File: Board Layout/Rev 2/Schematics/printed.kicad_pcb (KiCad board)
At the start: 2 copper layers, 5 parts

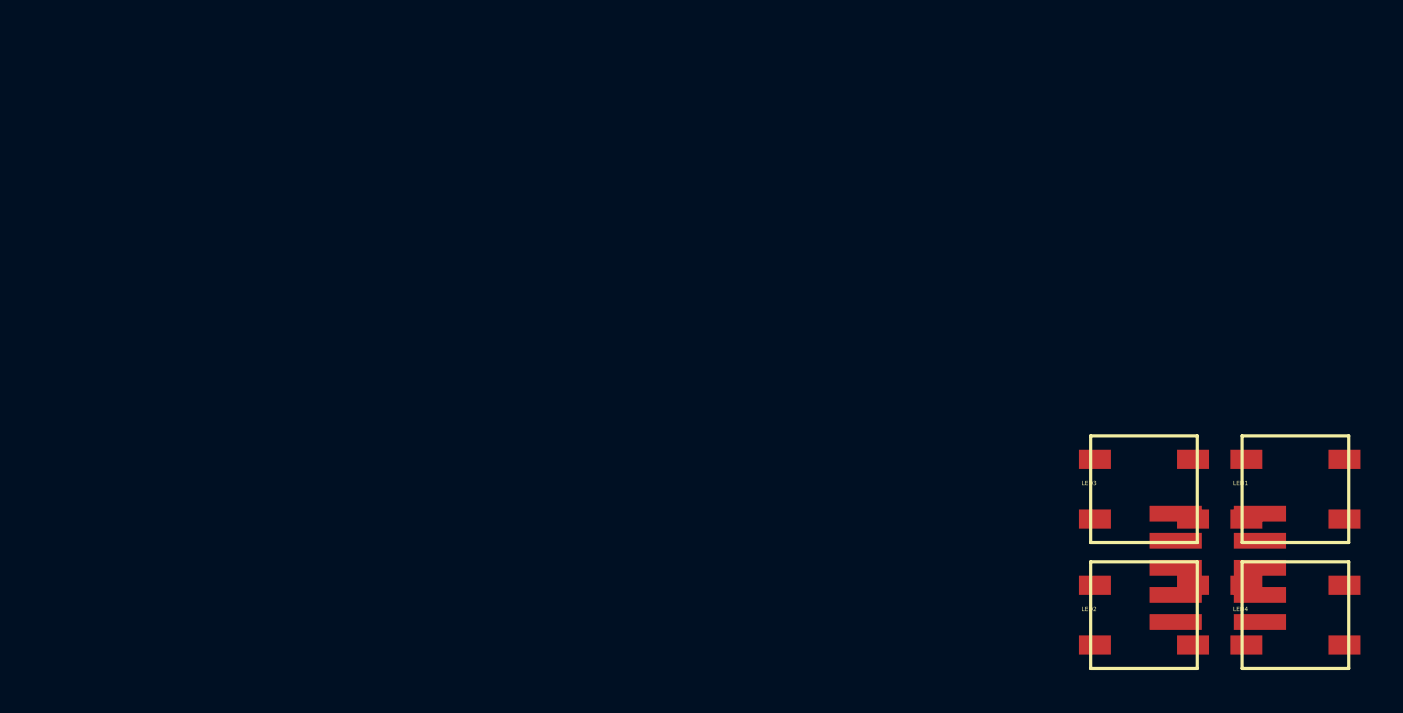
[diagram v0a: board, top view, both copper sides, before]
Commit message: Board Update
not sure if I can do 2 layer as it is too condensed. Might need to
switch to 4 layer.
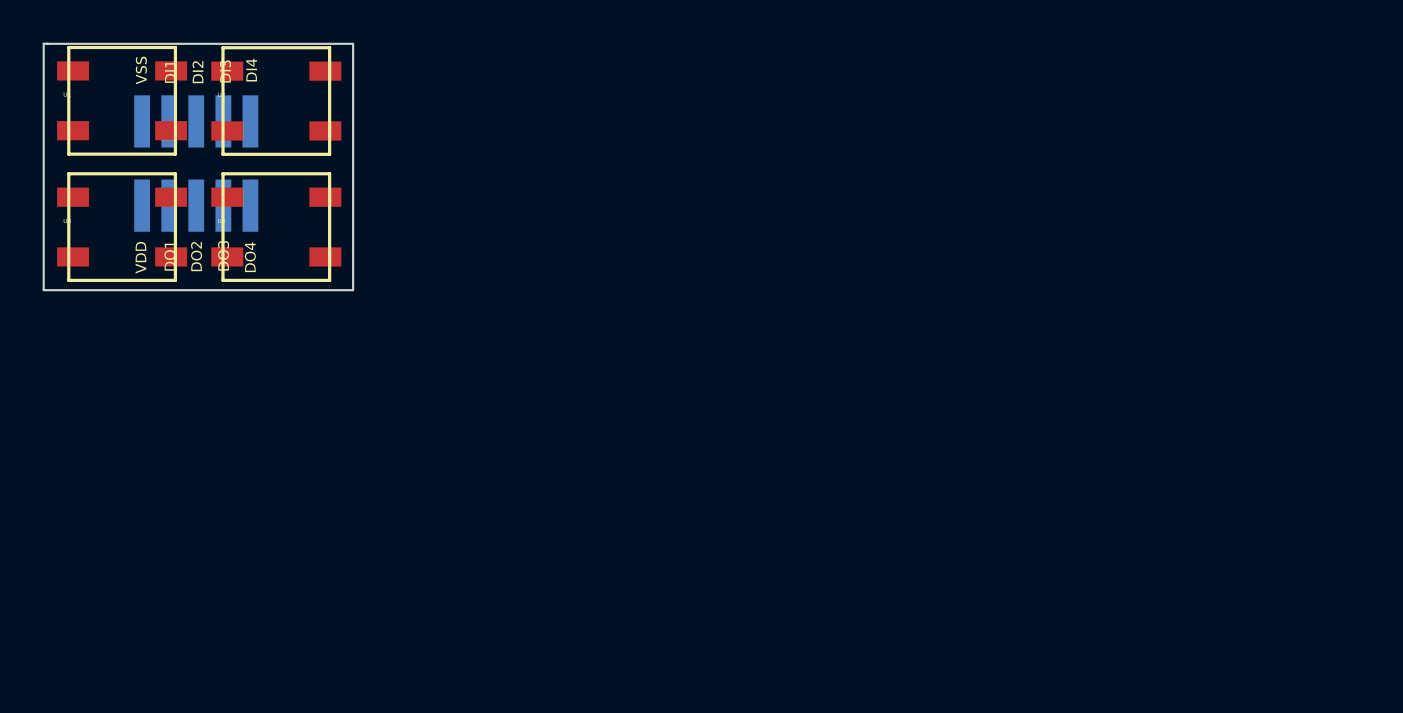
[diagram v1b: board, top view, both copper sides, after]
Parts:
- removed LED1, LED2, LED3, LED4: WS2812B, WS2812B
- added U1: , WS2812B, F.Cu at (118.8, 87.9)
- added U2: , WS2812B, F.Cu at (126.0, 87.9)
- added U3: , WS2812B, F.Cu at (118.8, 93.8)
- added U4: , WS2812B, F.Cu at (126.0, 93.8)
- ?: value CONN_5X2 -> (none); moved to F.Cu
- moved ? 48.7 mm to (128.0, 87.2), turned to 0 degrees
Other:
- board outline added: 14.5 x 11.6 mm

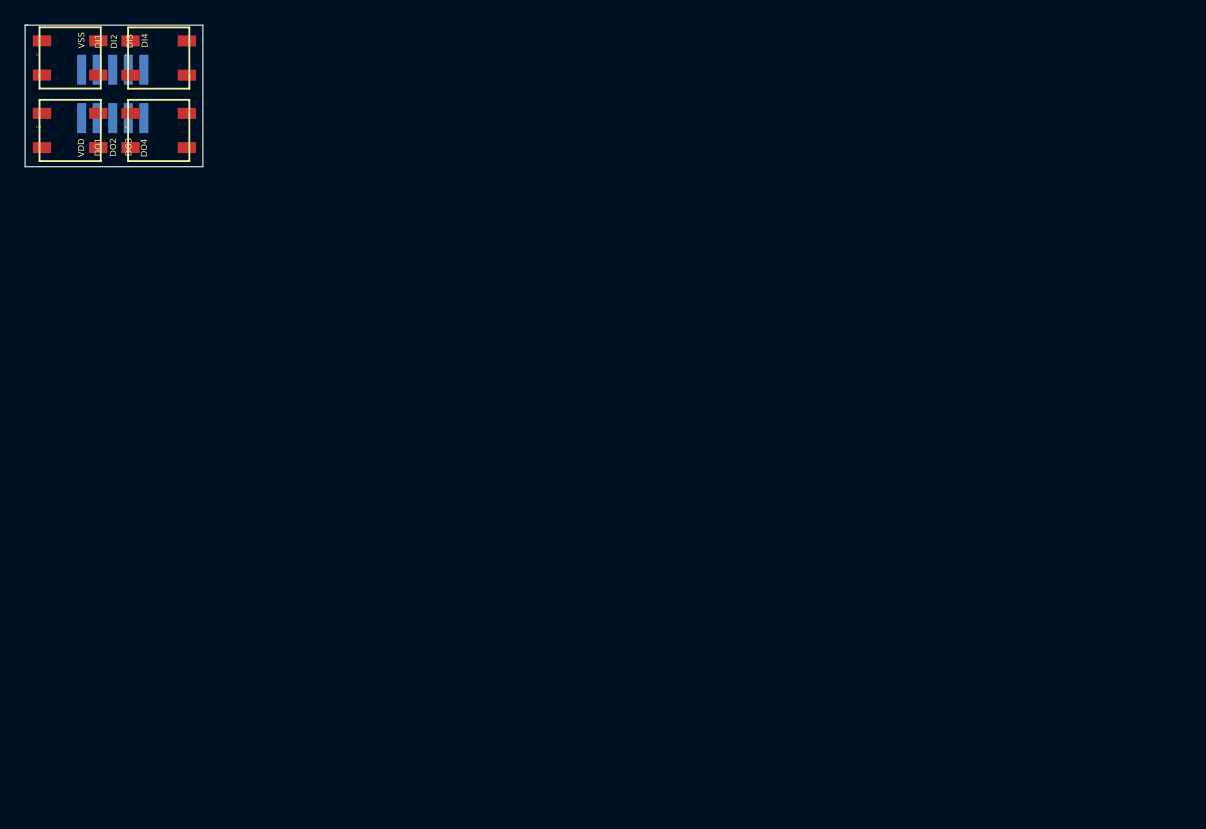
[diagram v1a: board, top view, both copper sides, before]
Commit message: Layout Completion
Verify design is fine via traces and via's; then order. Smaller than v1
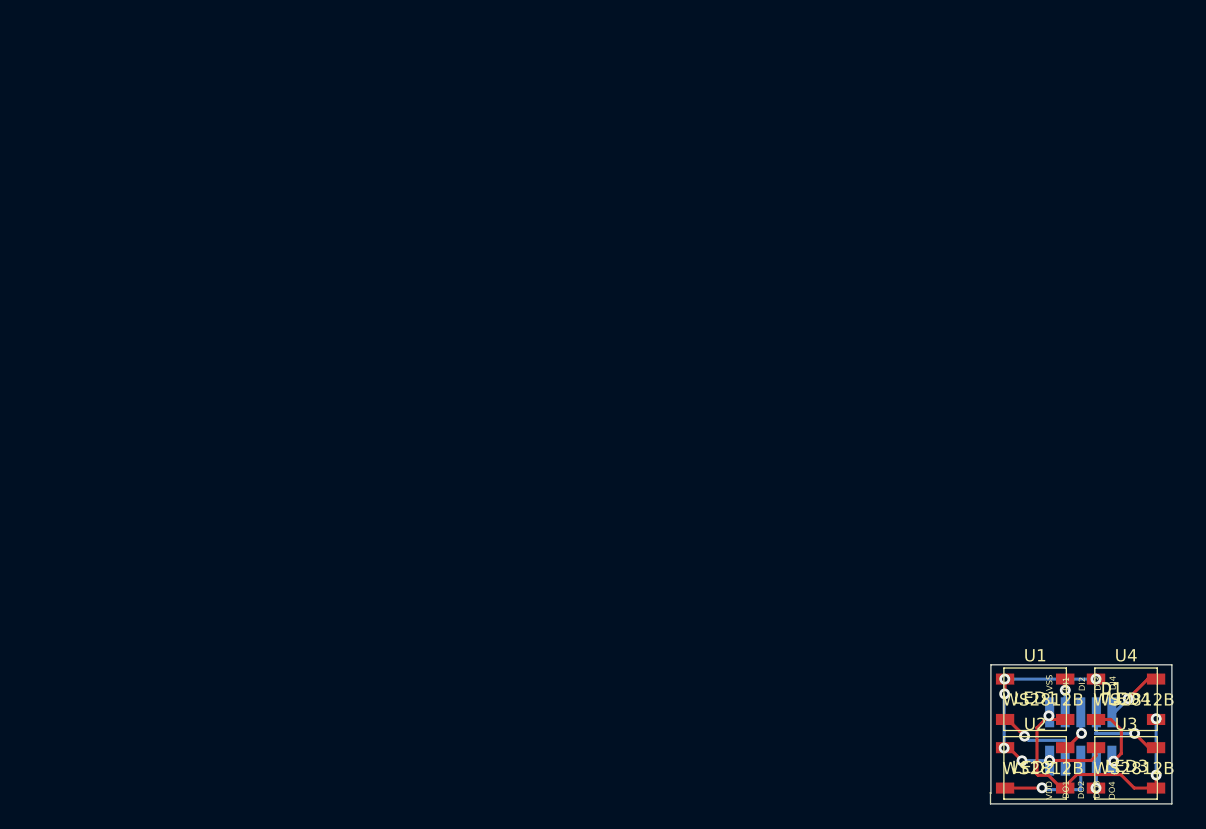
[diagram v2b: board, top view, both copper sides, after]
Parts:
- removed ?: , 10PSMTHdr
- added P1: CONN_5X2, 10PSMTHdr, F.Cu at (207.0, 139.7)
- U1, U2, U3, U4: value (none) -> WS2812B
- moved U3 101.6 mm to (207.5, 143.2)
- moved U1 95.4 mm to (200.1, 137.6)
- moved U4 92.6 mm to (207.5, 137.6)
- moved U2 92.5 mm to (200.1, 143.2)
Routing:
- net N-000006: track 0.00 -> 24.3 mm, vias 0 -> 3
- net N-0000010: track 0.00 -> 21.9 mm, vias 0 -> 6
- net N-000007: track 0.00 -> 8.60 mm, vias 0 -> 1
- net N-000009: track 0.00 -> 7.28 mm, vias 0 -> 1
- net N-000005: track 0.00 -> 7.18 mm, vias 0 -> 1
- net N-000003: track 0.00 -> 5.39 mm, vias 0 -> 1
- net N-000008: track 0.00 -> 4.73 mm, vias 0 -> 1
- net N-000002: track 0.00 -> 3.56 mm, vias 0 -> 1
- net N-000004: track 0.00 -> 2.72 mm, vias 0 -> 1
- net N-000001: track 0.00 -> 2.25 mm, vias 0 -> 1
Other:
- board size 14.5 x 11.6 mm -> 14.8 x 11.4 mm
- board text added: "DI1"
- board text added: "DI2"
- board text added: "DI3"
- board text added: "DI4"
- board text added: "DO1"
- board text added: "DO2"
- board text added: "DO3"
- board text added: "DO4"
- board text added: "LED1"
- board text added: "LED2"
- board text added: "LED3"
- board text added: "LED4"
- board text added: "VDD"
- board text added: "VSS"
